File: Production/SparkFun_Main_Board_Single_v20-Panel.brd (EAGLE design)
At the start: 186.9 x 176.3 mm, 510 parts, among them J1 MICROMOD-2222-C, J10 MICRO-SD-PUSH-PUSH-EXT-PIN, J11 Vertical Qwiic Connector, J14 QWIIC_RIGHT_ANGLE, J15 MICROMOD-2222-C, J18 CORTEX_JTAG_DEBUG_MINIMUM_PTH, J2 Vertical Qwiic Connector, J20 MICRO-SD-PUSH-PUSH-EXT-PIN, J21 MICROMOD_FUNCTION_MAIN, J25 Vertical Qwiic Connector, J26 QWIIC_RIGHT_ANGLE, J27 MICROMOD-2222-C, J30 CORTEX_JTAG_DEBUG_MINIMUM_PTH, J32 MICRO-SD-PUSH-PUSH-EXT-PIN, J33 MICROMOD_FUNCTION_MAIN, J37 Vertical Qwiic Connector, J38 QWIIC_RIGHT_ANGLE, J39 MICROMOD-2222-C, J4 QWIIC_RIGHT_ANGLE, J42 CORTEX_JTAG_DEBUG_MINIMUM_PTH, J44 MICRO-SD-PUSH-PUSH-EXT-PIN, J45 MICROMOD_FUNCTION_MAIN, J5 CORTEX_JTAG_DEBUG_MINIMUM_PTH, J6 MICROMOD_FUNCTION_MAIN, Q1 3.1A/30V/105mΩ, Q2 20V/4.2A/52mΩ/1.4W, Q3 3.1A/30V/105mΩ, Q4 20V/4.2A/52mΩ/1.4W, Q5 3.1A/30V/105mΩ, Q6 20V/4.2A/52mΩ/1.4W, Q7 3.1A/30V/105mΩ, Q8 20V/4.2A/52mΩ/1.4W, U1 STG3856QTR, U10 AP7347DQ-33W5-7K-3.3V, U11 MCP73831, U12 AP7361C-33, U13 STG3856QTR, U14 ESD Diode, U15 AP7347DQ-33W5-7K-3.3V, U16 MCP73831, U17 AP7361C-33, U18 STG3856QTR, U19 ESD Diode, U2 MCP73831, U20 AP7347DQ-33W5-7K-3.3V, U3 ESD Diode, U4 AP7347DQ-33W5-7K-3.3V, U5 AP7361C-33, U6 MCP73831, U7 AP7361C-33, U8 STG3856QTR, U9 ESD Diode

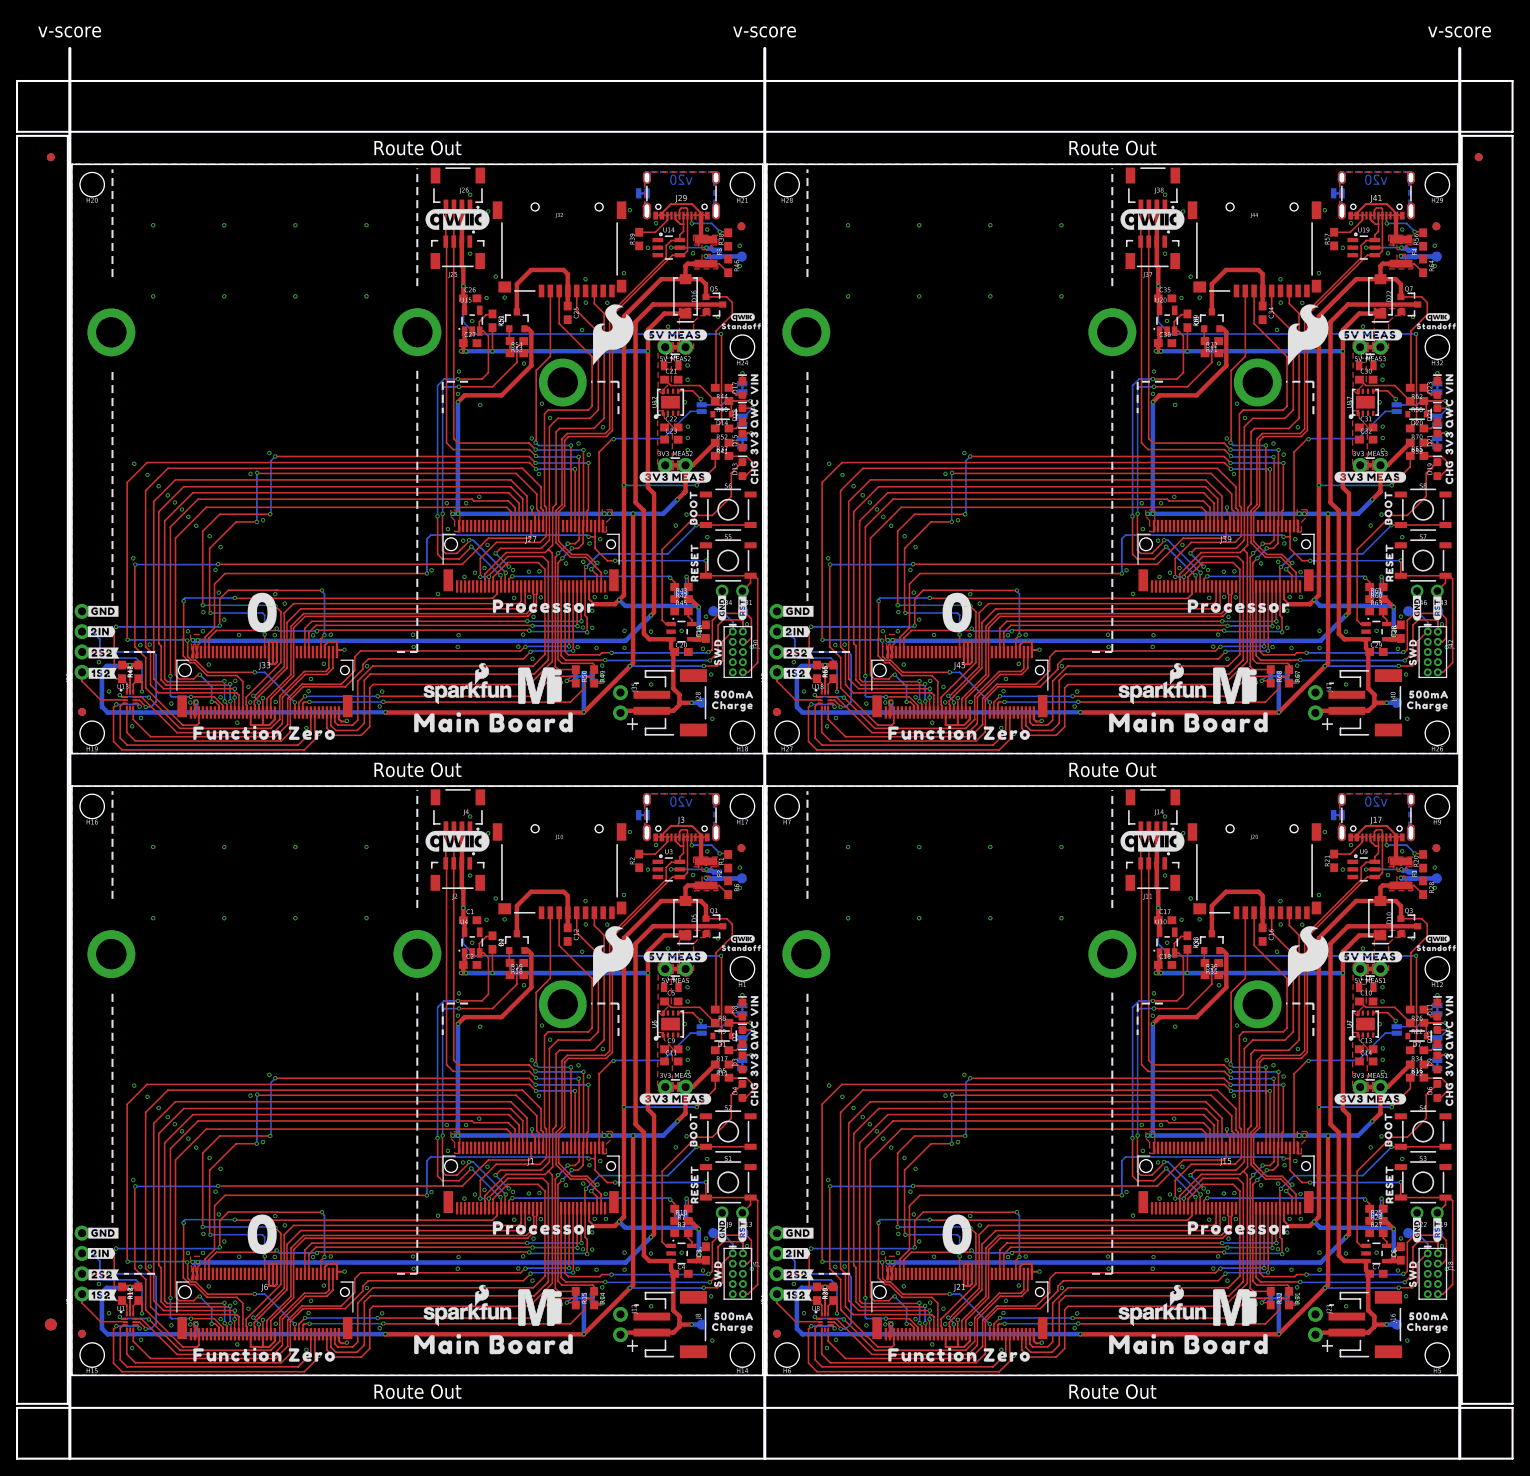
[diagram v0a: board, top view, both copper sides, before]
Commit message: Remakes production files
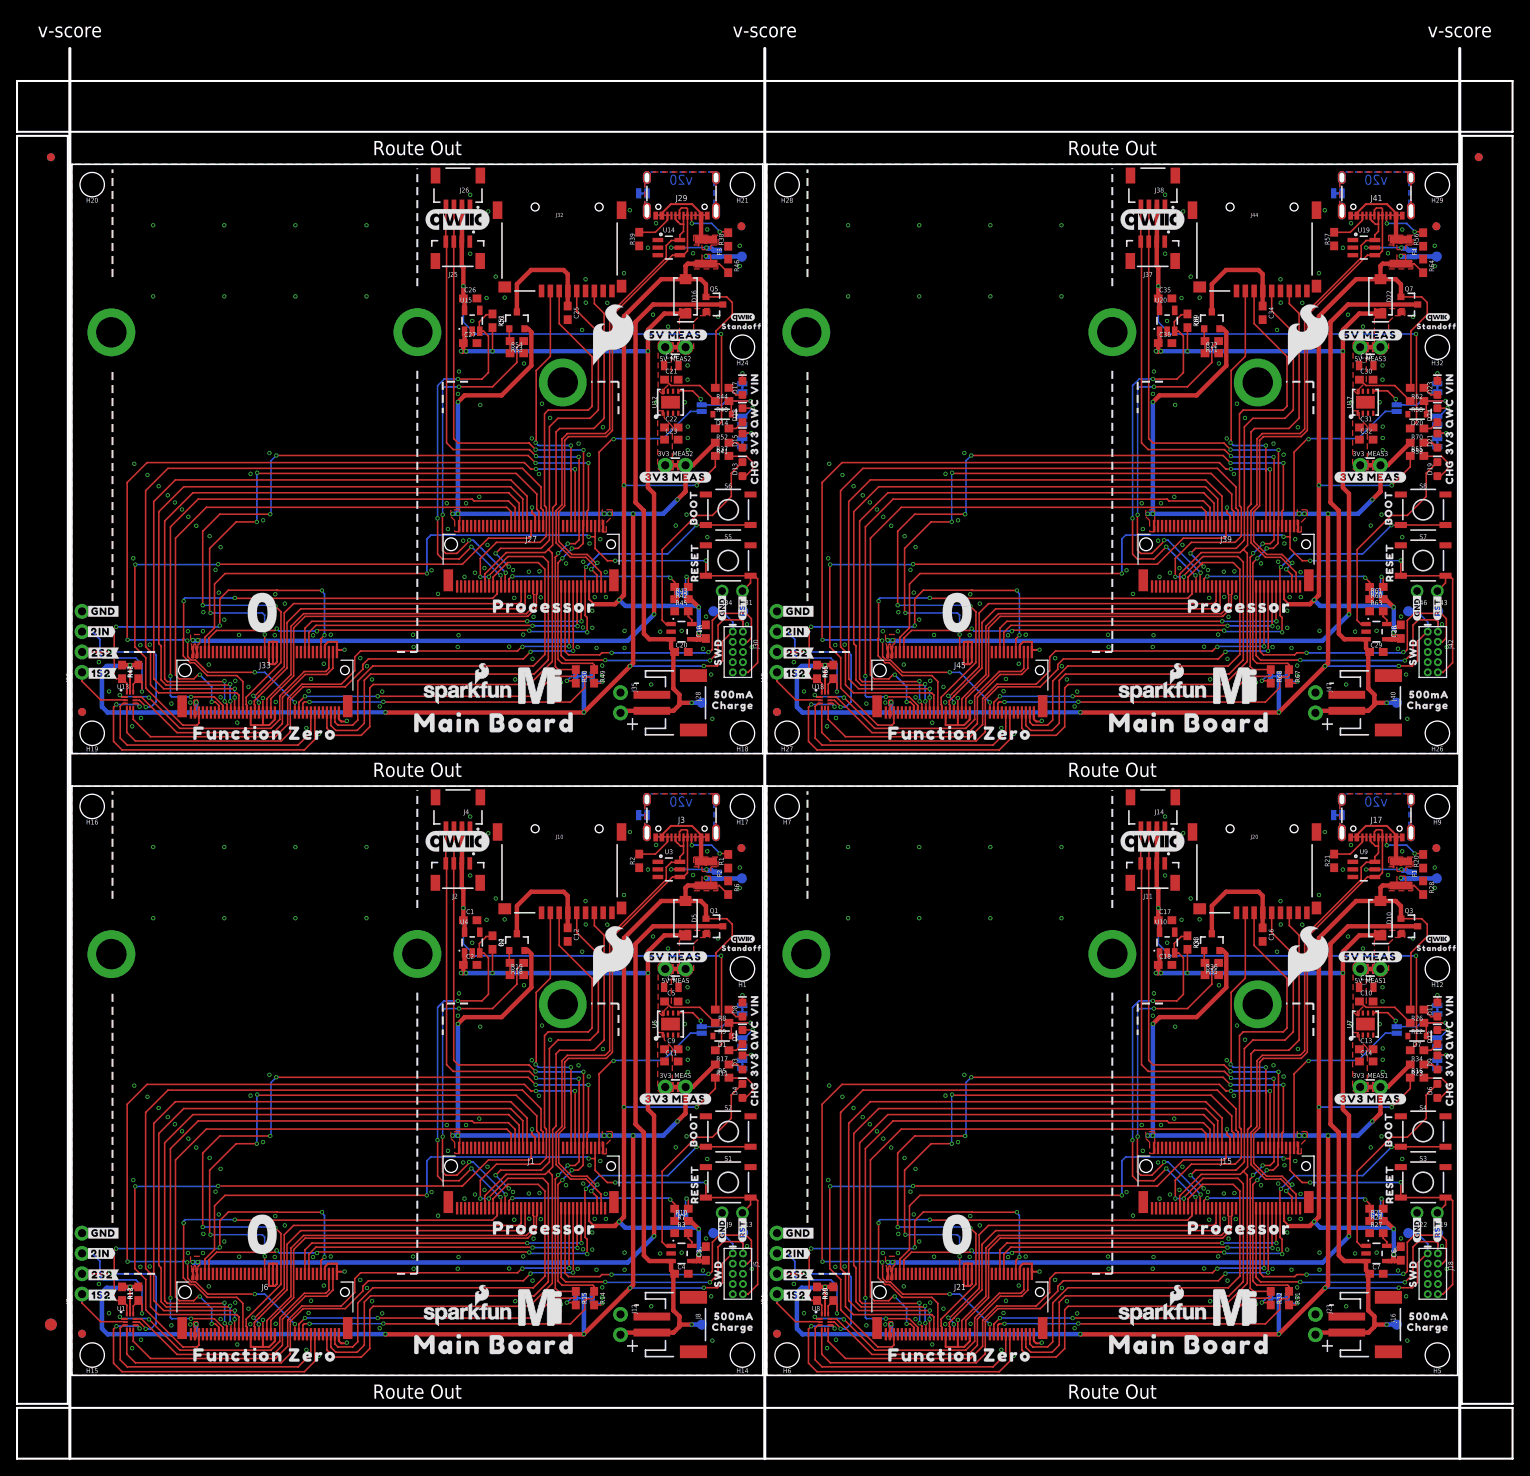
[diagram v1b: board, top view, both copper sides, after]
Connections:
- removed net !BOOT!: J1.11, J6.66, S2.3, S2.4
- removed net !BOOT!1: J15.11, J21.66, S4.3, S4.4
- removed net !BOOT!2: J27.11, J33.66, S6.3, S6.4
- removed net !BOOT!3: J39.11, J45.66, S8.3, S8.4
- removed net !CS0!-PROCESSOR: J1.55, J6.49
- removed net !CS0!-PROCESSOR1: J15.55, J21.49
- removed net !CS0!-PROCESSOR2: J27.55, J33.49
- removed net !CS0!-PROCESSOR3: J39.55, J45.49
- removed net !DFU-FC0!: J6.10, R13.2, U1.P12
- removed net !DFU-FC0!1: J21.10, R30.2, U8.P12
- removed net !DFU-FC0!2: J33.10, R48.2, U13.P12
- removed net !DFU-FC0!3: J45.10, R66.2, U18.P12
- removed net !RESET!: J1.6, J13.1, J5.10, J6.68, S1.3, S1.4
- removed net !RESET!1: J15.6, J18.10, J19.1, J21.68, S3.3, S3.4
- removed net !RESET!2: J27.6, J30.10, J31.1, J33.68, S5.3, S5.4
- removed net !RESET!3: J39.6, J42.10, J43.1, J45.68, S7.3, S7.4
- removed net 1S2_MULTIPLEXER: J7.1, U1.P2
- removed net 1S2_MULTIPLEXER1: J24.1, U8.P2
- removed net 1S2_MULTIPLEXER2: J36.1, U13.P2
- removed net 1S2_MULTIPLEXER3: J48.1, U18.P2
- removed net 2IN_MULTIPLEXER: J7.3, R12.1, U1.P10
- removed net 2IN_MULTIPLEXER1: J24.3, R29.1, U8.P10
- removed net 2IN_MULTIPLEXER2: J36.3, R47.1, U13.P10
- removed net 2IN_MULTIPLEXER3: J48.3, R65.1, U18.P10
- removed net 2S2_MULTIPLEXER: J7.2, U1.P8
- removed net 2S2_MULTIPLEXER1: J24.2, U8.P8
- removed net 2S2_MULTIPLEXER2: J36.2, U13.P8
- removed net 2S2_MULTIPLEXER3: J48.2, U18.P8
- removed net 3.3V: 3V3_MEAS.2, 3V3_MEAS.4, I2C_PU.2, J1.2, J1.74, J5.1, J6.73, Q2.2, R11.2, R12.2, R13.1, TP2.1, U1.P11
- removed net 3.3V1: 3V3_MEAS1.2, 3V3_MEAS1.4, I2C_PU1.2, J15.2, J15.74, J18.1, J21.73, Q4.2, R23.2, R29.2, R30.1, TP5.1, U8.P11
- removed net 3.3V2: 3V3_MEAS2.2, 3V3_MEAS2.4, I2C_PU2.2, J27.2, J27.74, J30.1, J33.73, Q6.2, R41.2, R47.2, R48.1, TP9.1, U13.P11
- removed net 3.3V3: 3V3_MEAS3.2, 3V3_MEAS3.4, I2C_PU3.2, J39.2, J39.74, J42.1, J45.73, Q8.2, R59.2, R65.2, R66.1, TP13.1, U18.P11
- removed net 3.3V_EN: J1.4, VE.1
- removed net 3.3V_EN1: J15.4, VE1.1
- removed net 3.3V_EN2: J27.4, VE2.1
- removed net 3.3V_EN3: J39.4, VE3.1
- removed net 3.3V_EN_VE: D1.C, R9.1, U5.5, VE.2
- removed net 3.3V_EN_VE1: D7.C, R22.1, U7.5, VE1.2
- removed net 3.3V_EN_VE2: D14.C, R40.1, U12.5, VE2.2
- removed net 3.3V_EN_VE3: D20.C, R58.1, U17.5, VE3.2
- removed net 3.3V_QWIIC: C1.1, J2.2, J4.2, R17.2, U4.5
- removed net 3.3V_QWIIC1: C17.1, J11.2, J14.2, R34.2, U10.5
- removed net 3.3V_QWIIC2: C26.1, J25.2, J26.2, R52.2, U15.5
- removed net 3.3V_QWIIC3: C35.1, J37.2, J38.2, R70.2, U20.5
- removed net 3V3_MEAS: 3V3_MEAS.1, 3V3_MEAS.3, C11.1, C9.1, U5.1
- removed net 3V3_MEAS1: 3V3_MEAS1.1, 3V3_MEAS1.3, C13.1, C14.1, U7.1
- removed net 3V3_MEAS2: 3V3_MEAS2.1, 3V3_MEAS2.3, C22.1, C23.1, U12.1
- removed net 3V3_MEAS3: 3V3_MEAS3.1, 3V3_MEAS3.3, C31.1, C32.1, U17.1
- removed net A0-PROCESSOR: J1.34, J6.38
- removed net A0-PROCESSOR1: J15.34, J21.38
- removed net A0-PROCESSOR2: J27.34, J33.38
- removed net A0-PROCESSOR3: J39.34, J45.38
- removed net CTS1-PROCESSOR: J1.15, J6.16
- removed net CTS1-PROCESSOR1: J15.15, J21.16
- removed net CTS1-PROCESSOR2: J27.15, J33.16
- removed net CTS1-PROCESSOR3: J39.15, J45.16
- removed net D+: J1.3, J3.A6, J3.B6, U3.6
- removed net D+1: J15.3, J17.A6, J17.B6, U9.6
- removed net D+2: J27.3, J29.A6, J29.B6, U14.6
- removed net D+3: J39.3, J41.A6, J41.B6, U19.6
- removed net D-: J1.5, J3.A7, J3.B7, U3.4
- removed net D-1: J15.5, J17.A7, J17.B7, U9.4
- removed net D-2: J27.5, J29.A7, J29.B7, U14.4
- removed net D-3: J39.5, J41.A7, J41.B7, U19.4
- removed net D0-PROCESSOR: J1.10, J6.47
- removed net D0-PROCESSOR1: J15.10, J21.47
- removed net D0-PROCESSOR2: J27.10, J33.47
- removed net D0-PROCESSOR3: J39.10, J45.47
- removed net D1-PROCESSOR/SD_CARD_!CS!: J1.18, J10.2
- removed net D1-PROCESSOR/SD_CARD_!CS!1: J15.18, J20.2
- removed net D1-PROCESSOR/SD_CARD_!CS!2: J27.18, J32.2
- removed net D1-PROCESSOR/SD_CARD_!CS!3: J39.18, J44.2
- removed net G0-PROCESSOR: J1.40, J6.53
- removed net G0-PROCESSOR1: J15.40, J21.53
- removed net G0-PROCESSOR2: J27.40, J33.53
- removed net G0-PROCESSOR3: J39.40, J45.53
- removed net G1-PROCESSOR: J1.42, J6.55
- removed net G1-PROCESSOR1: J15.42, J21.55
- removed net G1-PROCESSOR2: J27.42, J33.55
- removed net G1-PROCESSOR3: J39.42, J45.55
- removed net G2-PROCESSOR: J1.44, J6.57
- removed net G2-PROCESSOR1: J15.44, J21.57
- removed net G2-PROCESSOR2: J27.44, J33.57
- removed net G2-PROCESSOR3: J39.44, J45.57
- removed net G3-PROCESSOR: J1.46, J6.59
- removed net G3-PROCESSOR1: J15.46, J21.59
- removed net G3-PROCESSOR2: J27.46, J33.59
- removed net G3-PROCESSOR3: J39.46, J45.59
- removed net G4-PROCESSOR: J1.48, J6.61
- removed net G4-PROCESSOR1: J15.48, J21.61
- removed net G4-PROCESSOR2: J27.48, J33.61
- removed net G4-PROCESSOR3: J39.48, J45.61
- removed net GND: 3V3_LED.1, 5V_LED.1, C1.2, C11.2, C12.2, C2.2, C3.2, C4.2, C5.2, C8.2, C9.2, D1.A, DIVIDER.1, H2.1, H4.1, H8.1, J1.1, J1.33, J1.36, J1.39, J1.45, J1.7, J1.75, J10.10, J10.11, J10.12, J10.13, J10.6, J12.1, J2.1, J3.GND, J3.GND2, J4.1, J5.3, J5.5, J5.9, J6.1, J6.2, J6.32, J6.33, J6.34, J6.36, J6.39, J6.45, J6.75, J6.8, J7.4, J8.1, J9.1, QWIIC_LED.1, R1.1, R19.2, R2.1, R3.1, R6.1, S1.1, S1.2, S2.1, S2.2, SHLD.1, U1.P5, U2.2, U3.2, U4.2, U5.4, U5.EP
- removed net GND1: 3V3_LED1.1, 5V_LED1.1, C10.2, C13.2, C14.2, C15.2, C16.2, C17.2, C18.2, C6.2, C7.2, D7.A, DIVIDER1.1, H10.1, H11.1, H3.1, J11.1, J14.1, J15.1, J15.33, J15.36, J15.39, J15.45, J15.7, J15.75, J16.1, J17.GND, J17.GND2, J18.3, J18.5, J18.9, J20.10, J20.11, J20.12, J20.13, J20.6, J21.1, J21.2, J21.32, J21.33, J21.34, J21.36, J21.39, J21.45, J21.75, J21.8, J22.1, J23.1, J24.4, QWIIC_LED1.1, R20.1, R21.1, R27.1, R28.1, R36.2, S3.1, S3.2, S4.1, S4.2, SHLD1.1, U10.2, U6.2, U7.4, U7.EP, U8.P5, U9.2
- removed net GND2: 3V3_LED2.1, 5V_LED2.1, C19.2, C20.2, C21.2, C22.2, C23.2, C24.2, C25.2, C26.2, C27.2, D14.A, DIVIDER2.1, H13.1, H22.1, H23.1, J25.1, J26.1, J27.1, J27.33, J27.36, J27.39, J27.45, J27.7, J27.75, J28.1, J29.GND, J29.GND2, J30.3, J30.5, J30.9, J32.10, J32.11, J32.12, J32.13, J32.6, J33.1, J33.2, J33.32, J33.33, J33.34, J33.36, J33.39, J33.45, J33.75, J33.8, J34.1, J35.1, J36.4, QWIIC_LED2.1, R38.1, R39.1, R45.1, R46.1, R54.2, S5.1, S5.2, S6.1, S6.2, SHLD2.1, U11.2, U12.4, U12.EP, U13.P5, U14.2, U15.2
- removed net GND3: 3V3_LED3.1, 5V_LED3.1, C28.2, C29.2, C30.2, C31.2, C32.2, C33.2, C34.2, C35.2, C36.2, D20.A, DIVIDER3.1, H25.1, H30.1, H31.1, J37.1, J38.1, J39.1, J39.33, J39.36, J39.39, J39.45, J39.7, J39.75, J40.1, J41.GND, J41.GND2, J42.3, J42.5, J42.9, J44.10, J44.11, J44.12, J44.13, J44.6, J45.1, J45.2, J45.32, J45.33, J45.34, J45.36, J45.39, J45.45, J45.75, J45.8, J46.1, J47.1, J48.4, QWIIC_LED3.1, R56.1, R57.1, R63.1, R64.1, R72.2, S7.1, S7.2, S8.1, S8.2, SHLD3.1, U16.2, U17.4, U17.EP, U18.P5, U19.2, U20.2
- removed net HOST_D+: J1.35, J6.35
- removed net HOST_D+1: J15.35, J21.35
- removed net HOST_D+2: J27.35, J33.35
- removed net HOST_D+3: J39.35, J45.35
- removed net HOST_D-: J1.37, J6.37
- removed net HOST_D-1: J15.37, J21.37
- removed net HOST_D-2: J27.37, J33.37
- removed net HOST_D-3: J39.37, J45.37
- removed net I2C_!INT!: J1.16, J6.23
- removed net I2C_!INT!1: J15.16, J21.23
- removed net I2C_!INT!2: J27.16, J33.23
- removed net I2C_!INT!3: J39.16, J45.23
- removed net I2C_SCL: J1.14, J2.4, J4.4, J6.21, R15.1
- removed net I2C_SCL1: J11.4, J14.4, J15.14, J21.21, R32.1
- removed net I2C_SCL1-PROCESSOR/QWIIC_EN: J1.53, R4.1, U4.3
- removed net I2C_SCL1-PROCESSOR/QWIIC_EN1: J15.53, R33.1, U10.3
- removed net I2C_SCL1-PROCESSOR/QWIIC_EN2: J27.53, R51.1, U15.3
- removed net I2C_SCL1-PROCESSOR/QWIIC_EN3: J39.53, R69.1, U20.3
- removed net I2C_SCL2: J25.4, J26.4, J27.14, J33.21, R50.1
- removed net I2C_SCL3: J37.4, J38.4, J39.14, J45.21, R68.1
- removed net I2C_SDA: J1.12, J2.3, J4.3, J6.19, R14.1
- removed net I2C_SDA1: J11.3, J14.3, J15.12, J21.19, R31.1
- removed net I2C_SDA1-PROCESSOR/!SD_ENABLE!: J1.51, R18.1
- removed net I2C_SDA1-PROCESSOR/!SD_ENABLE!1: J15.51, R35.1
- removed net I2C_SDA1-PROCESSOR/!SD_ENABLE!2: J27.51, R53.1
- removed net I2C_SDA1-PROCESSOR/!SD_ENABLE!3: J39.51, R71.1
- removed net I2C_SDA2: J25.3, J26.3, J27.12, J33.19, R49.1
- removed net I2C_SDA3: J37.3, J38.3, J39.12, J45.19, R67.1
- removed net N$1: J17.B5, R21.2
- removed net N$10: 3V3_LED.2, D3.C
- removed net N$11: I2C_PU.3, R14.2
- removed net N$12: D8.A, R8.1
- removed net N$13: I2C_PU.1, R15.2
- removed net N$14: D2.A, R17.1
- removed net N$15: D2.C, QWIIC_LED.2
- removed net N$16: C12.1, J10.4, Q2.3
- removed net N$17: J17.A5, R20.2
- removed net N$18: Q2.1, R18.2, R19.1
- removed net N$19: D9.A, R23.1
- removed net N$2: 5V_LED.2, D8.C
- removed net N$20: D11.A, R26.1
- removed net N$21: 5V_LED1.2, D11.C
- removed net N$22: 3V3_LED1.2, D9.C
- removed net N$23: I2C_PU1.3, R31.2
- removed net N$24: I2C_PU1.1, R32.2
- removed net N$25: R27.2, U6.5
- removed net N$26: DIVIDER1.2, R24.1
- removed net N$27: D6.C, U6.1
- removed net N$28: D6.A, R16.2
- removed net N$29: D12.A, R34.1
- removed net N$3: D3.A, R11.1
- removed net N$30: D12.C, QWIIC_LED1.2
- removed net N$31: Q4.1, R35.2, R36.1
- removed net N$32: C16.1, J20.4, Q4.3
- removed net N$33: J29.B5, R39.2
- removed net N$34: J29.A5, R38.2
- removed net N$35: D15.A, R41.1
- removed net N$36: D17.A, R44.1
- removed net N$37: 5V_LED2.2, D17.C
- removed net N$38: 3V3_LED2.2, D15.C
- removed net N$39: I2C_PU2.3, R49.2
- removed net N$4: J3.B5, R2.2
- removed net N$40: I2C_PU2.1, R50.2
- removed net N$41: R45.2, U11.5
- removed net N$42: DIVIDER2.2, R42.1
- removed net N$43: D13.C, U11.1
- removed net N$44: D13.A, R37.2
- removed net N$45: D18.A, R52.1
- removed net N$46: D18.C, QWIIC_LED2.2
- removed net N$47: Q6.1, R53.2, R54.1
- removed net N$48: C25.1, J32.4, Q6.3
- removed net N$49: J41.B5, R57.2
- removed net N$5: J3.A5, R1.2
- removed net N$50: J41.A5, R56.2
- removed net N$51: D21.A, R59.1
- removed net N$52: D23.A, R62.1
- removed net N$53: 5V_LED3.2, D23.C
- removed net N$54: 3V3_LED3.2, D21.C
- removed net N$55: I2C_PU3.3, R67.2
- removed net N$56: I2C_PU3.1, R68.2
- removed net N$57: R63.2, U16.5
- removed net N$58: DIVIDER3.2, R60.1
- removed net N$59: D19.C, U16.1
- removed net N$6: R3.2, U2.5
- removed net N$60: D19.A, R55.2
- removed net N$61: D24.A, R70.1
- removed net N$62: D24.C, QWIIC_LED3.2
- removed net N$63: Q8.1, R71.2, R72.1
- removed net N$64: C34.1, J44.4, Q8.3
- removed net N$7: DIVIDER.2, R7.1
- removed net N$8: D4.C, U2.1
- removed net N$9: D4.A, R5.2
- removed net PROCESSOR_CAN-RX: J1.41, J6.43
- removed net PROCESSOR_CAN-RX1: J15.41, J21.43
- removed net PROCESSOR_CAN-RX2: J27.41, J33.43
- removed net PROCESSOR_CAN-RX3: J39.41, J45.43
- removed net PROCESSOR_CAN-TX: J1.43, J6.41
- removed net PROCESSOR_CAN-TX1: J15.43, J21.41
- removed net PROCESSOR_CAN-TX2: J27.43, J33.41
- removed net PROCESSOR_CAN-TX3: J39.43, J45.41
- removed net PWM0-PROCESSOR: J1.32, J6.51
- removed net PWM0-PROCESSOR1: J15.32, J21.51
- removed net PWM0-PROCESSOR2: J27.32, J33.51
- removed net PWM0-PROCESSOR3: J39.32, J45.51
- removed net PWR_EN0: J1.38, J6.71
- removed net PWR_EN1: J15.38, J21.71
- removed net PWR_EN2: J27.38, J33.71
- removed net PWR_EN3: J39.38, J45.71
- removed net RTS1-PROCESSOR: J1.13, J6.18
- removed net RTS1-PROCESSOR1: J15.13, J21.18
- removed net RTS1-PROCESSOR2: J27.13, J33.18
- removed net RTS1-PROCESSOR3: J39.13, J45.18
- removed net RX1-DFU_TX-FC0-PLEX: J6.4, U1.P9
- removed net RX1-DFU_TX-FC0-PLEX1: J21.4, U8.P9
- removed net RX1-DFU_TX-FC0-PLEX2: J33.4, U13.P9
- removed net RX1-DFU_TX-FC0-PLEX3: J45.4, U18.P9
- removed net RX1-PROCESSOR: J1.19, U1.P6
- removed net RX1-PROCESSOR-PLEX: J6.13, U1.P7
- removed net RX1-PROCESSOR-PLEX1: J21.13, U8.P7
- removed net RX1-PROCESSOR-PLEX2: J33.13, U13.P7
- removed net RX1-PROCESSOR-PLEX3: J45.13, U18.P7
- removed net RX1-PROCESSOR1: J15.19, U8.P6
- removed net RX1-PROCESSOR2: J27.19, U13.P6
- removed net RX1-PROCESSOR3: J39.19, U18.P6
- removed net SHLD: J3.SHLD1, J3.SHLD2, J3.SHLD3, J3.SHLD4, SHLD.2
- removed net SHLD1: J17.SHLD1, J17.SHLD2, J17.SHLD3, J17.SHLD4, SHLD1.2
- removed net SHLD2: J29.SHLD1, J29.SHLD2, J29.SHLD3, J29.SHLD4, SHLD2.2
- removed net SHLD3: J41.SHLD1, J41.SHLD2, J41.SHLD3, J41.SHLD4, SHLD3.2
- removed net SPI_PROCESSOR_SCK: J1.57, J10.5, J6.3
- removed net SPI_PROCESSOR_SCK1: J15.57, J20.5, J21.3
- removed net SPI_PROCESSOR_SCK2: J27.57, J32.5, J33.3
- removed net SPI_PROCESSOR_SCK3: J39.57, J44.5, J45.3
- removed net SPI_PROCESSOR_SDI: J1.61, J10.7, J6.7
- removed net SPI_PROCESSOR_SDI1: J15.61, J20.7, J21.7
- removed net SPI_PROCESSOR_SDI2: J27.61, J32.7, J33.7
- removed net SPI_PROCESSOR_SDI3: J39.61, J44.7, J45.7
- removed net SPI_PROCESSOR_SDO: J1.59, J10.3, J6.5
- removed net SPI_PROCESSOR_SDO1: J15.59, J20.3, J21.5
- removed net SPI_PROCESSOR_SDO2: J27.59, J32.3, J33.5
- removed net SPI_PROCESSOR_SDO3: J39.59, J44.3, J45.5
- removed net SWDCK: J1.21, J5.4
- removed net SWDCK1: J15.21, J18.4
- removed net SWDCK2: J27.21, J30.4
- removed net SWDCK3: J39.21, J42.4
- removed net SWDIO: J1.23, J5.2, TP1.1
- removed net SWDIO1: J15.23, J18.2, TP8.1
- removed net SWDIO2: J27.23, J30.2, TP12.1
- removed net SWDIO3: J39.23, J42.2, TP16.1
- removed net TX1-DFU_RX-FC0-PLEX: J6.6, U1.P1
- removed net TX1-DFU_RX-FC0-PLEX1: J21.6, U8.P1
- removed net TX1-DFU_RX-FC0-PLEX2: J33.6, U13.P1
- removed net TX1-DFU_RX-FC0-PLEX3: J45.6, U18.P1
- removed net TX1-PROCESSOR: J1.17, U1.P4
- removed net TX1-PROCESSOR-PLEX: J6.15, U1.P3
- removed net TX1-PROCESSOR-PLEX1: J21.15, U8.P3
- removed net TX1-PROCESSOR-PLEX2: J33.15, U13.P3
- removed net TX1-PROCESSOR-PLEX3: J45.15, U18.P3
- removed net TX1-PROCESSOR1: J15.17, U8.P4
- removed net TX1-PROCESSOR2: J27.17, U13.P4
- removed net TX1-PROCESSOR3: J39.17, U18.P4
- removed net VCC: 5V_MEAS.1, 5V_MEAS.3, C2.1, D5.C, J6.72, J6.74, Q1.2, R4.2, U4.1
- removed net VCC1: 5V_MEAS1.1, 5V_MEAS1.3, C18.1, D10.C, J21.72, J21.74, Q3.2, R33.2, U10.1
- removed net VCC2: 5V_MEAS2.1, 5V_MEAS2.3, C27.1, D16.C, J33.72, J33.74, Q5.2, R51.2, U15.1
- removed net VCC3: 5V_MEAS3.1, 5V_MEAS3.3, C36.1, D22.C, J45.72, J45.74, Q7.2, R69.2, U20.1
- removed net VCC_MEAS: 5V_MEAS.2, 5V_MEAS.4, C5.1, C8.1, R9.2, U5.8
- removed net VCC_MEAS1: 5V_MEAS1.2, 5V_MEAS1.4, C10.1, C15.1, R22.2, U7.8
- removed net VCC_MEAS2: 5V_MEAS2.2, 5V_MEAS2.4, C21.1, C24.1, R40.2, U12.8
- removed net VCC_MEAS3: 5V_MEAS3.2, 5V_MEAS3.4, C30.1, C33.1, R58.2, U17.8
- removed net VIN: BYP.2, C3.1, D5.A, F2.2, J1.9, Q1.1, R10.2, R5.1, R6.2, R8.2, TP4.1, U2.4
- removed net VIN/1: J15.49, R24.2, R25.1
- removed net VIN/2: J27.49, R42.2, R43.1
- removed net VIN/3: J1.49, R10.1, R7.2
- removed net VIN/4: J39.49, R60.2, R61.1
- removed net VIN1: BYP1.2, C6.1, D10.A, F1.2, J15.9, Q3.1, R16.1, R25.2, R26.2, R28.2, TP7.1, U6.4
- removed net VIN2: BYP2.2, C19.1, D16.A, F3.2, J27.9, Q5.1, R37.1, R43.2, R44.2, R46.2, TP11.1, U11.4
- removed net VIN3: BYP3.2, C28.1, D22.A, F4.2, J39.9, Q7.1, R55.1, R61.2, R62.2, R64.2, TP15.1, U16.4
- removed net V_BATT: C4.1, J12.2, J8.2, Q1.3, TP3.1, U2.3
- removed net V_BATT1: C7.1, J16.2, J23.2, Q3.3, TP6.1, U6.3
- removed net V_BATT2: C20.1, J28.2, J35.2, Q5.3, TP10.1, U11.3
- removed net V_BATT3: C29.1, J40.2, J47.2, Q7.3, TP14.1, U16.3
- removed net V_USB: BYP.1, F2.1, J3.VBUS1, J3.VBUS2, U3.5
- removed net V_USB1: BYP1.1, F1.1, J17.VBUS1, J17.VBUS2, U9.5
- removed net V_USB2: BYP2.1, F3.1, J29.VBUS1, J29.VBUS2, U14.5
- removed net V_USB3: BYP3.1, F4.1, J41.VBUS1, J41.VBUS2, U19.5
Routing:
- net GND3: vias 157 -> 161
- net GND2: vias 157 -> 161
- net GND1: vias 157 -> 161
- net GND: vias 157 -> 161

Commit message: Updates production files
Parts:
- U$1: device top:#1S2#3 -> top:#TXO#7
- U$116, U$158, U$74: device top:#1S2#3 -> top:#GND#3
- U$117, U$159, U$75: device top:#2S2#3 -> top:#GND#3
- U$118, U$160, U$76: device top:#2IN#0 -> top:SWD6522
- U$119, U$161, U$77: device top:#GND#3 -> SparkFun-Aesthetics:SFE_LOGO_NAME_FLAME_.1
- U$12: device top:#2IN#0 -> top:##SEL##5
- U$120, U$162, U$78: device bot:#1S2#3 -> top:QWC4
- U$121, U$163, U$79: device bot:#2IN#0 -> top:#TXO#7
- U$122, U$164, U$80: device bot:#2S2#3 -> top:#RXI#6
- U$123, U$165, U$81: device top:#GND#3 -> top:##SEL##5
- U$124, U$166, U$82: device top:SWD6522 -> bot:##SEL##3
- U$125, U$167, U$83: device SparkFun-Aesthetics:SFE_LOGO_NAME_FLAME_.1 -> bot:#RXI#4
- U$126, U$168, U$84: device top:QWC4 -> bot:#TXO#5
- U$19: device bot:#1S2#3 -> bot:##SEL##3
- U$2: device top:#2S2#3 -> top:#RXI#6
- U$20: device bot:#2IN#0 -> bot:#RXI#4
- U$28: device bot:#2S2#3 -> bot:#TXO#5
- moved U$120 87.9 mm to (85.3, 120.3), flipped to the top, turned to 90 degrees
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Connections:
- new net !BOOT!: J1.11, J6.66, S2.3, S2.4
- new net !BOOT!1: J15.11, J21.66, S4.3, S4.4
- new net !BOOT!2: J27.11, J33.66, S6.3, S6.4
- new net !BOOT!3: J39.11, J45.66, S8.3, S8.4
- new net !CS0!-PROCESSOR: J1.55, J6.49
- new net !CS0!-PROCESSOR1: J15.55, J21.49
- new net !CS0!-PROCESSOR2: J27.55, J33.49
- new net !CS0!-PROCESSOR3: J39.55, J45.49
- new net !DFU-FC0!: J6.10, R13.2, U1.P12
- new net !DFU-FC0!1: J21.10, R30.2, U8.P12
- new net !DFU-FC0!2: J33.10, R48.2, U13.P12
- new net !DFU-FC0!3: J45.10, R66.2, U18.P12
- new net !RESET!: J1.6, J13.1, J5.10, J6.68, S1.3, S1.4
- new net !RESET!1: J15.6, J18.10, J19.1, J21.68, S3.3, S3.4
- new net !RESET!2: J27.6, J30.10, J31.1, J33.68, S5.3, S5.4
- new net !RESET!3: J39.6, J42.10, J43.1, J45.68, S7.3, S7.4
- new net !SEL!/2IN: J7.3, R12.1, U1.P10
- new net !SEL!/2IN1: J24.3, R29.1, U8.P10
- new net !SEL!/2IN2: J36.3, R47.1, U13.P10
- new net !SEL!/2IN3: J48.3, R65.1, U18.P10
- new net 3.3V: 3V3_MEAS.2, 3V3_MEAS.4, I2C_PU.2, J1.2, J1.74, J5.1, J6.73, Q2.2, R11.2, R12.2, R13.1, TP2.1, U1.P11
- new net 3.3V1: 3V3_MEAS1.2, 3V3_MEAS1.4, I2C_PU1.2, J15.2, J15.74, J18.1, J21.73, Q4.2, R23.2, R29.2, R30.1, TP5.1, U8.P11
- new net 3.3V2: 3V3_MEAS2.2, 3V3_MEAS2.4, I2C_PU2.2, J27.2, J27.74, J30.1, J33.73, Q6.2, R41.2, R47.2, R48.1, TP9.1, U13.P11
- new net 3.3V3: 3V3_MEAS3.2, 3V3_MEAS3.4, I2C_PU3.2, J39.2, J39.74, J42.1, J45.73, Q8.2, R59.2, R65.2, R66.1, TP13.1, U18.P11
- new net 3.3V_EN: J1.4, VE.1
- new net 3.3V_EN1: J15.4, VE1.1
- new net 3.3V_EN2: J27.4, VE2.1
- new net 3.3V_EN3: J39.4, VE3.1
- new net 3.3V_EN_VE: D1.C, R9.1, U5.5, VE.2
- new net 3.3V_EN_VE1: D7.C, R22.1, U7.5, VE1.2
- new net 3.3V_EN_VE2: D14.C, R40.1, U12.5, VE2.2
- new net 3.3V_EN_VE3: D20.C, R58.1, U17.5, VE3.2
- new net 3.3V_QWIIC: C1.1, J2.2, J4.2, R17.2, U4.5
- new net 3.3V_QWIIC1: C17.1, J11.2, J14.2, R34.2, U10.5
- new net 3.3V_QWIIC2: C26.1, J25.2, J26.2, R52.2, U15.5
- new net 3.3V_QWIIC3: C35.1, J37.2, J38.2, R70.2, U20.5
- new net 3V3_MEAS: 3V3_MEAS.1, 3V3_MEAS.3, C11.1, C9.1, U5.1
- new net 3V3_MEAS1: 3V3_MEAS1.1, 3V3_MEAS1.3, C13.1, C14.1, U7.1
- new net 3V3_MEAS2: 3V3_MEAS2.1, 3V3_MEAS2.3, C22.1, C23.1, U12.1
- new net 3V3_MEAS3: 3V3_MEAS3.1, 3V3_MEAS3.3, C31.1, C32.1, U17.1
- new net A0-PROCESSOR: J1.34, J6.38
- new net A0-PROCESSOR1: J15.34, J21.38
- new net A0-PROCESSOR2: J27.34, J33.38
- new net A0-PROCESSOR3: J39.34, J45.38
- new net CTS1-PROCESSOR: J1.15, J6.16
- new net CTS1-PROCESSOR1: J15.15, J21.16
- new net CTS1-PROCESSOR2: J27.15, J33.16
- new net CTS1-PROCESSOR3: J39.15, J45.16
- new net D+: J1.3, J3.A6, J3.B6, U3.6
- new net D+1: J15.3, J17.A6, J17.B6, U9.6
- new net D+2: J27.3, J29.A6, J29.B6, U14.6
- new net D+3: J39.3, J41.A6, J41.B6, U19.6
- new net D-: J1.5, J3.A7, J3.B7, U3.4
- new net D-1: J15.5, J17.A7, J17.B7, U9.4
- new net D-2: J27.5, J29.A7, J29.B7, U14.4
- new net D-3: J39.5, J41.A7, J41.B7, U19.4
- new net D0-PROCESSOR: J1.10, J6.47
- new net D0-PROCESSOR1: J15.10, J21.47
- new net D0-PROCESSOR2: J27.10, J33.47
- new net D0-PROCESSOR3: J39.10, J45.47
- new net D1-PROCESSOR/SD_CARD_!CS!: J1.18, J10.2
- new net D1-PROCESSOR/SD_CARD_!CS!1: J15.18, J20.2
- new net D1-PROCESSOR/SD_CARD_!CS!2: J27.18, J32.2
- new net D1-PROCESSOR/SD_CARD_!CS!3: J39.18, J44.2
- new net G0-PROCESSOR: J1.40, J6.53
- new net G0-PROCESSOR1: J15.40, J21.53
- new net G0-PROCESSOR2: J27.40, J33.53
- new net G0-PROCESSOR3: J39.40, J45.53
- new net G1-PROCESSOR: J1.42, J6.55
- new net G1-PROCESSOR1: J15.42, J21.55
- new net G1-PROCESSOR2: J27.42, J33.55
- new net G1-PROCESSOR3: J39.42, J45.55
- new net G2-PROCESSOR: J1.44, J6.57
- new net G2-PROCESSOR1: J15.44, J21.57
- new net G2-PROCESSOR2: J27.44, J33.57
- new net G2-PROCESSOR3: J39.44, J45.57
- new net G3-PROCESSOR: J1.46, J6.59
- new net G3-PROCESSOR1: J15.46, J21.59
- new net G3-PROCESSOR2: J27.46, J33.59
- new net G3-PROCESSOR3: J39.46, J45.59
- new net G4-PROCESSOR: J1.48, J6.61
- new net G4-PROCESSOR1: J15.48, J21.61
- new net G4-PROCESSOR2: J27.48, J33.61
- new net G4-PROCESSOR3: J39.48, J45.61
- new net GND: 3V3_LED.1, 5V_LED.1, C1.2, C11.2, C12.2, C2.2, C3.2, C4.2, C5.2, C8.2, C9.2, D1.A, DIVIDER.1, H2.1, H4.1, H8.1, J1.1, J1.33, J1.36, J1.39, J1.45, J1.7, J1.75, J10.10, J10.11, J10.12, J10.13, J10.6, J12.1, J2.1, J3.GND, J3.GND2, J4.1, J5.3, J5.5, J5.9, J6.1, J6.2, J6.32, J6.33, J6.34, J6.36, J6.39, J6.45, J6.75, J6.8, J7.4, J8.1, J9.1, QWIIC_LED.1, R1.1, R19.2, R2.1, R3.1, R6.1, S1.1, S1.2, S2.1, S2.2, SHLD.1, U1.P5, U2.2, U3.2, U4.2, U5.4, U5.EP
- new net GND1: 3V3_LED1.1, 5V_LED1.1, C10.2, C13.2, C14.2, C15.2, C16.2, C17.2, C18.2, C6.2, C7.2, D7.A, DIVIDER1.1, H10.1, H11.1, H3.1, J11.1, J14.1, J15.1, J15.33, J15.36, J15.39, J15.45, J15.7, J15.75, J16.1, J17.GND, J17.GND2, J18.3, J18.5, J18.9, J20.10, J20.11, J20.12, J20.13, J20.6, J21.1, J21.2, J21.32, J21.33, J21.34, J21.36, J21.39, J21.45, J21.75, J21.8, J22.1, J23.1, J24.4, QWIIC_LED1.1, R20.1, R21.1, R27.1, R28.1, R36.2, S3.1, S3.2, S4.1, S4.2, SHLD1.1, U10.2, U6.2, U7.4, U7.EP, U8.P5, U9.2
- new net GND2: 3V3_LED2.1, 5V_LED2.1, C19.2, C20.2, C21.2, C22.2, C23.2, C24.2, C25.2, C26.2, C27.2, D14.A, DIVIDER2.1, H13.1, H22.1, H23.1, J25.1, J26.1, J27.1, J27.33, J27.36, J27.39, J27.45, J27.7, J27.75, J28.1, J29.GND, J29.GND2, J30.3, J30.5, J30.9, J32.10, J32.11, J32.12, J32.13, J32.6, J33.1, J33.2, J33.32, J33.33, J33.34, J33.36, J33.39, J33.45, J33.75, J33.8, J34.1, J35.1, J36.4, QWIIC_LED2.1, R38.1, R39.1, R45.1, R46.1, R54.2, S5.1, S5.2, S6.1, S6.2, SHLD2.1, U11.2, U12.4, U12.EP, U13.P5, U14.2, U15.2
- new net GND3: 3V3_LED3.1, 5V_LED3.1, C28.2, C29.2, C30.2, C31.2, C32.2, C33.2, C34.2, C35.2, C36.2, D20.A, DIVIDER3.1, H25.1, H30.1, H31.1, J37.1, J38.1, J39.1, J39.33, J39.36, J39.39, J39.45, J39.7, J39.75, J40.1, J41.GND, J41.GND2, J42.3, J42.5, J42.9, J44.10, J44.11, J44.12, J44.13, J44.6, J45.1, J45.2, J45.32, J45.33, J45.34, J45.36, J45.39, J45.45, J45.75, J45.8, J46.1, J47.1, J48.4, QWIIC_LED3.1, R56.1, R57.1, R63.1, R64.1, R72.2, S7.1, S7.2, S8.1, S8.2, SHLD3.1, U16.2, U17.4, U17.EP, U18.P5, U19.2, U20.2
- new net HOST_D+: J1.35, J6.35
- new net HOST_D+1: J15.35, J21.35
- new net HOST_D+2: J27.35, J33.35
- new net HOST_D+3: J39.35, J45.35
- new net HOST_D-: J1.37, J6.37
- new net HOST_D-1: J15.37, J21.37
- new net HOST_D-2: J27.37, J33.37
- new net HOST_D-3: J39.37, J45.37
- new net I2C_!INT!: J1.16, J6.23
- new net I2C_!INT!1: J15.16, J21.23
- new net I2C_!INT!2: J27.16, J33.23
- new net I2C_!INT!3: J39.16, J45.23
- new net I2C_SCL: J1.14, J2.4, J4.4, J6.21, R15.1
- new net I2C_SCL1: J11.4, J14.4, J15.14, J21.21, R32.1
- new net I2C_SCL1-PROCESSOR/QWIIC_EN: J1.53, R4.1, U4.3
- new net I2C_SCL1-PROCESSOR/QWIIC_EN1: J15.53, R33.1, U10.3
- new net I2C_SCL1-PROCESSOR/QWIIC_EN2: J27.53, R51.1, U15.3
- new net I2C_SCL1-PROCESSOR/QWIIC_EN3: J39.53, R69.1, U20.3
- new net I2C_SCL2: J25.4, J26.4, J27.14, J33.21, R50.1
- new net I2C_SCL3: J37.4, J38.4, J39.14, J45.21, R68.1
- new net I2C_SDA: J1.12, J2.3, J4.3, J6.19, R14.1
- new net I2C_SDA1: J11.3, J14.3, J15.12, J21.19, R31.1
- new net I2C_SDA1-PROCESSOR/!SD_ENABLE!: J1.51, R18.1
- new net I2C_SDA1-PROCESSOR/!SD_ENABLE!1: J15.51, R35.1
- new net I2C_SDA1-PROCESSOR/!SD_ENABLE!2: J27.51, R53.1
- new net I2C_SDA1-PROCESSOR/!SD_ENABLE!3: J39.51, R71.1
- new net I2C_SDA2: J25.3, J26.3, J27.12, J33.19, R49.1
- new net I2C_SDA3: J37.3, J38.3, J39.12, J45.19, R67.1
- new net N$1: J17.B5, R21.2
- new net N$10: 3V3_LED.2, D3.C
- new net N$11: I2C_PU.3, R14.2
- new net N$12: D8.A, R8.1
- new net N$13: I2C_PU.1, R15.2
- new net N$14: D2.A, R17.1
- new net N$15: D2.C, QWIIC_LED.2
- new net N$16: C12.1, J10.4, Q2.3
- new net N$17: J17.A5, R20.2
- new net N$18: Q2.1, R18.2, R19.1
- new net N$19: D9.A, R23.1
- new net N$2: 5V_LED.2, D8.C
- new net N$20: D11.A, R26.1
- new net N$21: 5V_LED1.2, D11.C
- new net N$22: 3V3_LED1.2, D9.C
- new net N$23: I2C_PU1.3, R31.2
- new net N$24: I2C_PU1.1, R32.2
- new net N$25: R27.2, U6.5
- new net N$26: DIVIDER1.2, R24.1
- new net N$27: D6.C, U6.1
- new net N$28: D6.A, R16.2
- new net N$29: D12.A, R34.1
- new net N$3: D3.A, R11.1
- new net N$30: D12.C, QWIIC_LED1.2
- new net N$31: Q4.1, R35.2, R36.1
- new net N$32: C16.1, J20.4, Q4.3
- new net N$33: J29.B5, R39.2
- new net N$34: J29.A5, R38.2
- new net N$35: D15.A, R41.1
- new net N$36: D17.A, R44.1
- new net N$37: 5V_LED2.2, D17.C
- new net N$38: 3V3_LED2.2, D15.C
- new net N$39: I2C_PU2.3, R49.2
- new net N$4: J3.B5, R2.2
- new net N$40: I2C_PU2.1, R50.2
- new net N$41: R45.2, U11.5
- new net N$42: DIVIDER2.2, R42.1
- new net N$43: D13.C, U11.1
- new net N$44: D13.A, R37.2
- new net N$45: D18.A, R52.1
- new net N$46: D18.C, QWIIC_LED2.2
- new net N$47: Q6.1, R53.2, R54.1
- new net N$48: C25.1, J32.4, Q6.3
- new net N$49: J41.B5, R57.2
- new net N$5: J3.A5, R1.2
- new net N$50: J41.A5, R56.2
- new net N$51: D21.A, R59.1
- new net N$52: D23.A, R62.1
- new net N$53: 5V_LED3.2, D23.C
- new net N$54: 3V3_LED3.2, D21.C
- new net N$55: I2C_PU3.3, R67.2
- new net N$56: I2C_PU3.1, R68.2
- new net N$57: R63.2, U16.5
- new net N$58: DIVIDER3.2, R60.1
- new net N$59: D19.C, U16.1
- new net N$6: R3.2, U2.5
- new net N$60: D19.A, R55.2
- new net N$61: D24.A, R70.1
- new net N$62: D24.C, QWIIC_LED3.2
- new net N$63: Q8.1, R71.2, R72.1
- new net N$64: C34.1, J44.4, Q8.3
- new net N$7: DIVIDER.2, R7.1
- new net N$8: D4.C, U2.1
- new net N$9: D4.A, R5.2
- new net PROCESSOR_CAN-RX: J1.41, J6.43
- new net PROCESSOR_CAN-RX1: J15.41, J21.43
- new net PROCESSOR_CAN-RX2: J27.41, J33.43
- new net PROCESSOR_CAN-RX3: J39.41, J45.43
- new net PROCESSOR_CAN-TX: J1.43, J6.41
- new net PROCESSOR_CAN-TX1: J15.43, J21.41
- new net PROCESSOR_CAN-TX2: J27.43, J33.41
- new net PROCESSOR_CAN-TX3: J39.43, J45.41
- new net PWM0-PROCESSOR: J1.32, J6.51
- new net PWM0-PROCESSOR1: J15.32, J21.51
- new net PWM0-PROCESSOR2: J27.32, J33.51
- new net PWM0-PROCESSOR3: J39.32, J45.51
- new net PWR_EN0: J1.38, J6.71
- new net PWR_EN1: J15.38, J21.71
- new net PWR_EN2: J27.38, J33.71
- new net PWR_EN3: J39.38, J45.71
- new net RTS1-PROCESSOR: J1.13, J6.18
- new net RTS1-PROCESSOR1: J15.13, J21.18
- new net RTS1-PROCESSOR2: J27.13, J33.18
- new net RTS1-PROCESSOR3: J39.13, J45.18
- new net RX1-DFU_TX-FC0-PLEX: J6.4, U1.P9
- new net RX1-DFU_TX-FC0-PLEX1: J21.4, U8.P9
- new net RX1-DFU_TX-FC0-PLEX2: J33.4, U13.P9
- new net RX1-DFU_TX-FC0-PLEX3: J45.4, U18.P9
- new net RX1-PROCESSOR: J1.19, U1.P6
- new net RX1-PROCESSOR-PLEX: J6.13, U1.P7
- new net RX1-PROCESSOR-PLEX1: J21.13, U8.P7
- new net RX1-PROCESSOR-PLEX2: J33.13, U13.P7
- new net RX1-PROCESSOR-PLEX3: J45.13, U18.P7
- new net RX1-PROCESSOR1: J15.19, U8.P6
- new net RX1-PROCESSOR2: J27.19, U13.P6
- new net RX1-PROCESSOR3: J39.19, U18.P6
- new net RX1/2S1: J24.2, U8.P8
- new net RX1/2S2: J7.2, U1.P8
- new net RX1/2S3: J36.2, U13.P8
- new net RX1/2S4: J48.2, U18.P8
- new net SHLD: J3.SHLD1, J3.SHLD2, J3.SHLD3, J3.SHLD4, SHLD.2
- new net SHLD1: J17.SHLD1, J17.SHLD2, J17.SHLD3, J17.SHLD4, SHLD1.2
- new net SHLD2: J29.SHLD1, J29.SHLD2, J29.SHLD3, J29.SHLD4, SHLD2.2
- new net SHLD3: J41.SHLD1, J41.SHLD2, J41.SHLD3, J41.SHLD4, SHLD3.2
- new net SPI_PROCESSOR_SCK: J1.57, J10.5, J6.3
- new net SPI_PROCESSOR_SCK1: J15.57, J20.5, J21.3
- new net SPI_PROCESSOR_SCK2: J27.57, J32.5, J33.3
- new net SPI_PROCESSOR_SCK3: J39.57, J44.5, J45.3
- new net SPI_PROCESSOR_SDI: J1.61, J10.7, J6.7
- new net SPI_PROCESSOR_SDI1: J15.61, J20.7, J21.7
- new net SPI_PROCESSOR_SDI2: J27.61, J32.7, J33.7
- new net SPI_PROCESSOR_SDI3: J39.61, J44.7, J45.7
- new net SPI_PROCESSOR_SDO: J1.59, J10.3, J6.5
- new net SPI_PROCESSOR_SDO1: J15.59, J20.3, J21.5
- new net SPI_PROCESSOR_SDO2: J27.59, J32.3, J33.5
- new net SPI_PROCESSOR_SDO3: J39.59, J44.3, J45.5
- new net SWDCK: J1.21, J5.4
- new net SWDCK1: J15.21, J18.4
- new net SWDCK2: J27.21, J30.4
- new net SWDCK3: J39.21, J42.4
- new net SWDIO: J1.23, J5.2, TP1.1
- new net SWDIO1: J15.23, J18.2, TP8.1
- new net SWDIO2: J27.23, J30.2, TP12.1
- new net SWDIO3: J39.23, J42.2, TP16.1
- new net TX1-DFU_RX-FC0-PLEX: J6.6, U1.P1
- new net TX1-DFU_RX-FC0-PLEX1: J21.6, U8.P1
- new net TX1-DFU_RX-FC0-PLEX2: J33.6, U13.P1
- new net TX1-DFU_RX-FC0-PLEX3: J45.6, U18.P1
- new net TX1-PROCESSOR: J1.17, U1.P4
- new net TX1-PROCESSOR-PLEX: J6.15, U1.P3
- new net TX1-PROCESSOR-PLEX1: J21.15, U8.P3
- new net TX1-PROCESSOR-PLEX2: J33.15, U13.P3
- new net TX1-PROCESSOR-PLEX3: J45.15, U18.P3
- new net TX1-PROCESSOR1: J15.17, U8.P4
- new net TX1-PROCESSOR2: J27.17, U13.P4
- new net TX1-PROCESSOR3: J39.17, U18.P4
- new net TX1/1S1: J24.1, U8.P2
- new net TX1/1S2: J7.1, U1.P2
- new net TX1/1S3: J36.1, U13.P2
- new net TX1/1S4: J48.1, U18.P2
- new net VCC: 5V_MEAS.1, 5V_MEAS.3, C2.1, D5.C, J6.72, J6.74, Q1.2, R4.2, U4.1
- new net VCC1: 5V_MEAS1.1, 5V_MEAS1.3, C18.1, D10.C, J21.72, J21.74, Q3.2, R33.2, U10.1
- new net VCC2: 5V_MEAS2.1, 5V_MEAS2.3, C27.1, D16.C, J33.72, J33.74, Q5.2, R51.2, U15.1
- new net VCC3: 5V_MEAS3.1, 5V_MEAS3.3, C36.1, D22.C, J45.72, J45.74, Q7.2, R69.2, U20.1
- new net VCC_MEAS: 5V_MEAS.2, 5V_MEAS.4, C5.1, C8.1, R9.2, U5.8
- new net VCC_MEAS1: 5V_MEAS1.2, 5V_MEAS1.4, C10.1, C15.1, R22.2, U7.8
- new net VCC_MEAS2: 5V_MEAS2.2, 5V_MEAS2.4, C21.1, C24.1, R40.2, U12.8
- new net VCC_MEAS3: 5V_MEAS3.2, 5V_MEAS3.4, C30.1, C33.1, R58.2, U17.8
- new net VIN: BYP.2, C3.1, D5.A, F2.2, J1.9, Q1.1, R10.2, R5.1, R6.2, R8.2, TP4.1, U2.4
- new net VIN/1: J15.49, R24.2, R25.1
- new net VIN/2: J27.49, R42.2, R43.1
- new net VIN/3: J1.49, R10.1, R7.2
- new net VIN/4: J39.49, R60.2, R61.1
- new net VIN1: BYP1.2, C6.1, D10.A, F1.2, J15.9, Q3.1, R16.1, R25.2, R26.2, R28.2, TP7.1, U6.4
- new net VIN2: BYP2.2, C19.1, D16.A, F3.2, J27.9, Q5.1, R37.1, R43.2, R44.2, R46.2, TP11.1, U11.4
- new net VIN3: BYP3.2, C28.1, D22.A, F4.2, J39.9, Q7.1, R55.1, R61.2, R62.2, R64.2, TP15.1, U16.4
- new net V_BATT: C4.1, J12.2, J8.2, Q1.3, TP3.1, U2.3
- new net V_BATT1: C7.1, J16.2, J23.2, Q3.3, TP6.1, U6.3
- new net V_BATT2: C20.1, J28.2, J35.2, Q5.3, TP10.1, U11.3
- new net V_BATT3: C29.1, J40.2, J47.2, Q7.3, TP14.1, U16.3
- new net V_USB: BYP.1, F2.1, J3.VBUS1, J3.VBUS2, U3.5
- new net V_USB1: BYP1.1, F1.1, J17.VBUS1, J17.VBUS2, U9.5
- new net V_USB2: BYP2.1, F3.1, J29.VBUS1, J29.VBUS2, U14.5
- new net V_USB3: BYP3.1, F4.1, J41.VBUS1, J41.VBUS2, U19.5
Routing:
- net 2S2_MULTIPLEXER3: track 18.7 -> 0.00 mm, vias 2 -> 0
- net 2S2_MULTIPLEXER2: track 18.7 -> 0.00 mm, vias 2 -> 0
- net 2S2_MULTIPLEXER1: track 18.7 -> 0.00 mm, vias 2 -> 0
- net 2S2_MULTIPLEXER: track 18.7 -> 0.00 mm, vias 2 -> 0
- net RX1/2S4: track 0.00 -> 18.6 mm, vias 0 -> 2
- net RX1/2S3: track 0.00 -> 18.6 mm, vias 0 -> 2
- net RX1/2S1: track 0.00 -> 18.6 mm, vias 0 -> 2
- net RX1/2S2: track 0.00 -> 18.6 mm, vias 0 -> 2
- net 2IN_MULTIPLEXER: track 17.5 -> 0.00 mm, vias 1 -> 0
- net !SEL!/2IN: track 0.00 -> 17.5 mm, vias 0 -> 1
- net 2IN_MULTIPLEXER2: track 17.5 -> 0.00 mm, vias 1 -> 0
- net !SEL!/2IN2: track 0.00 -> 17.5 mm, vias 0 -> 1
- net 2IN_MULTIPLEXER1: track 17.5 -> 0.00 mm, vias 1 -> 0
- net !SEL!/2IN1: track 0.00 -> 17.5 mm, vias 0 -> 1
- net 2IN_MULTIPLEXER3: track 17.5 -> 0.00 mm, vias 1 -> 0
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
